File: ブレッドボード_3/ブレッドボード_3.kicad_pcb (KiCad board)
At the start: 2 copper layers, 100 x 23.5 mm, 12 parts, among them J1 Conn_01x12_Socket, J10 XIAO_Rudder, J11 XIAO_Under, J2 BNO055, J3 SD_0, J4 GPS, J5 Conn_01x12_Socket, J6 ICS, J7 Conn_01x08_Socket, J8 ICS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

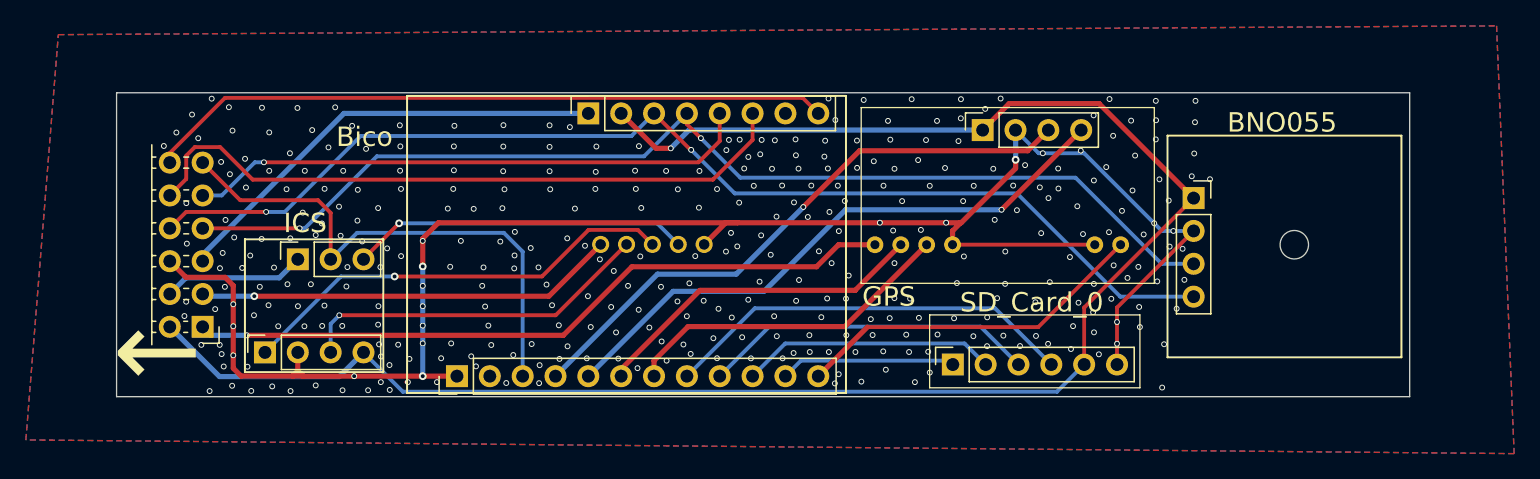
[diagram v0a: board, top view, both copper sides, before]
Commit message: change Conn 5P to 6P
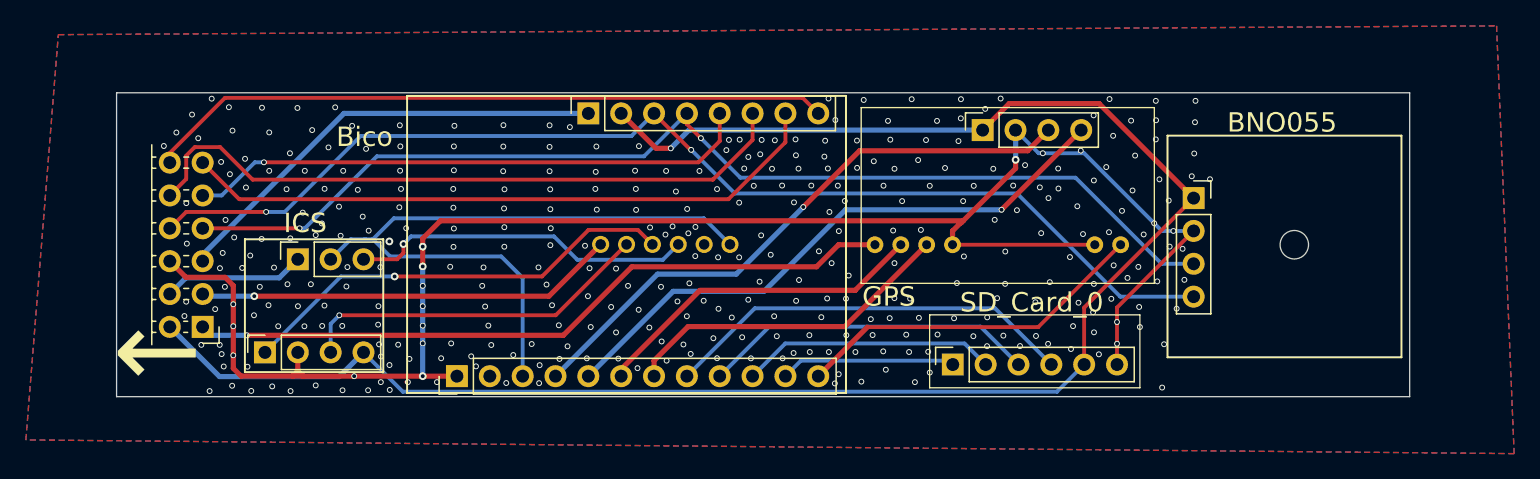
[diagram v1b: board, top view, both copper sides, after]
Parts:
- J10: footprint ブレッドボード_3:CONN5_B05B-PASK_JST -> ブレッドボード_3:CONN_B06B-PASK_JST
- moved J10 2.00 mm to (144.4, 144.7)
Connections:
- J1 pad 11: /SIG_ICS -> /RX_ESP
- J10 pad 1: /DC_GND -> /SIG_ICS
- J10 pad 2: /EN_ICS -> /DC_GND
- J10 pad 3: /RX_ICS -> /EN_ICS
- J10 pad 4: /TX_ICS -> /RX_ICS
- J10 pad 5: /5V_DC_Rudder -> /TX_ICS
- J7 pad 7: unconnected-(J7-Pin_7-Pad7) -> /RX_ESP
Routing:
- net /RX_ESP: track 0.00 -> 50.3 mm
- net /SIG_ICS: track 41.0 -> 53.4 mm
- net /DC_GND: track 140.7 -> 137.7 mm, vias 363 -> 361

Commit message: 家のPCで更新
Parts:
- added J12: SIG_ICS, ブレッドボード_3:CONN_B02B-PASK-1_JST, B.Cu at (132.5, 144.7)
- J10: footprint ブレッドボード_3:CONN_B06B-PASK_JST -> ブレッドボード_3:CONN_B05B-PASK_JST
- moved J10 3.59 mm to (148.0, 144.7)
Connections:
- J10 pad 1: /SIG_ICS -> /DC_GND
- J10 pad 2: /DC_GND -> /EN_ICS
- J10 pad 3: /EN_ICS -> /RX_ICS
- J10 pad 4: /RX_ICS -> /TX_ICS
- J10 pad 5: /TX_ICS -> /5V_DC_Rudder
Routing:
- net /SIG_ICS: track 53.4 -> 32.5 mm
- net /TX_ICS: track 27.6 -> 33.2 mm
- net /RX_ICS: track 34.3 -> 39.9 mm
- net /5V_DC_Rudder: track 32.5 -> 38.1 mm
- net /EN_ICS: track 26.7 -> 31.4 mm, vias 1 -> 2
- net /DC_GND: track 137.7 -> 138.7 mm, vias 361 -> 325
